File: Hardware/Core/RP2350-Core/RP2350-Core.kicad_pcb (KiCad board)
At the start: 2 copper layers, 9.1 x 7 mm, 60 parts, among them CN10 PR5L4015-5P-C-F, CN11 PR5L4015-5P-C-F, CN7 PR5L4015-5P-C-F, CN8 PR5L4015-5P-C-F, CN9 PR5L4015-5P-C-F, J7 SWD, J8 USB_C_Receptacle_USB2.0_14P, Q1 BSS123, Q3 BSS123, SW1 TS-1187A-B-A-B, SW2 TS-1187A-B-A-B, U1 RP2354B, U19 W25Q16JVSNIQ, U2 AP2112K-3.3, U3 LM66200DRLR, U35 PR5L5015-5P-C-H, U36 PR5L5015-5P-C-H, U37 PR5L5015-5P-C-H, U38 PR5L5015-5P-C-H, U39 PR5L5015-5P-C-H, Y1 Crystal

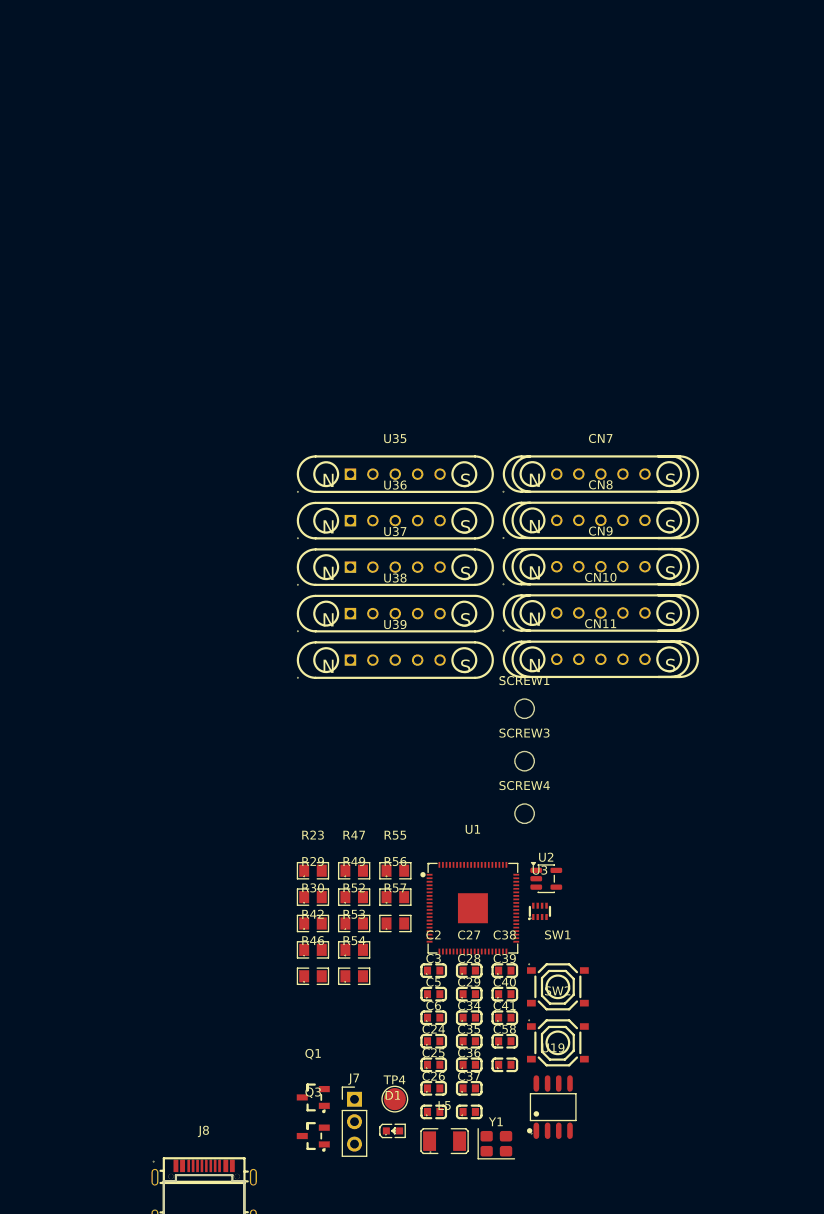
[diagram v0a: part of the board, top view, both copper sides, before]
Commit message: Footprint assigned core rp2350
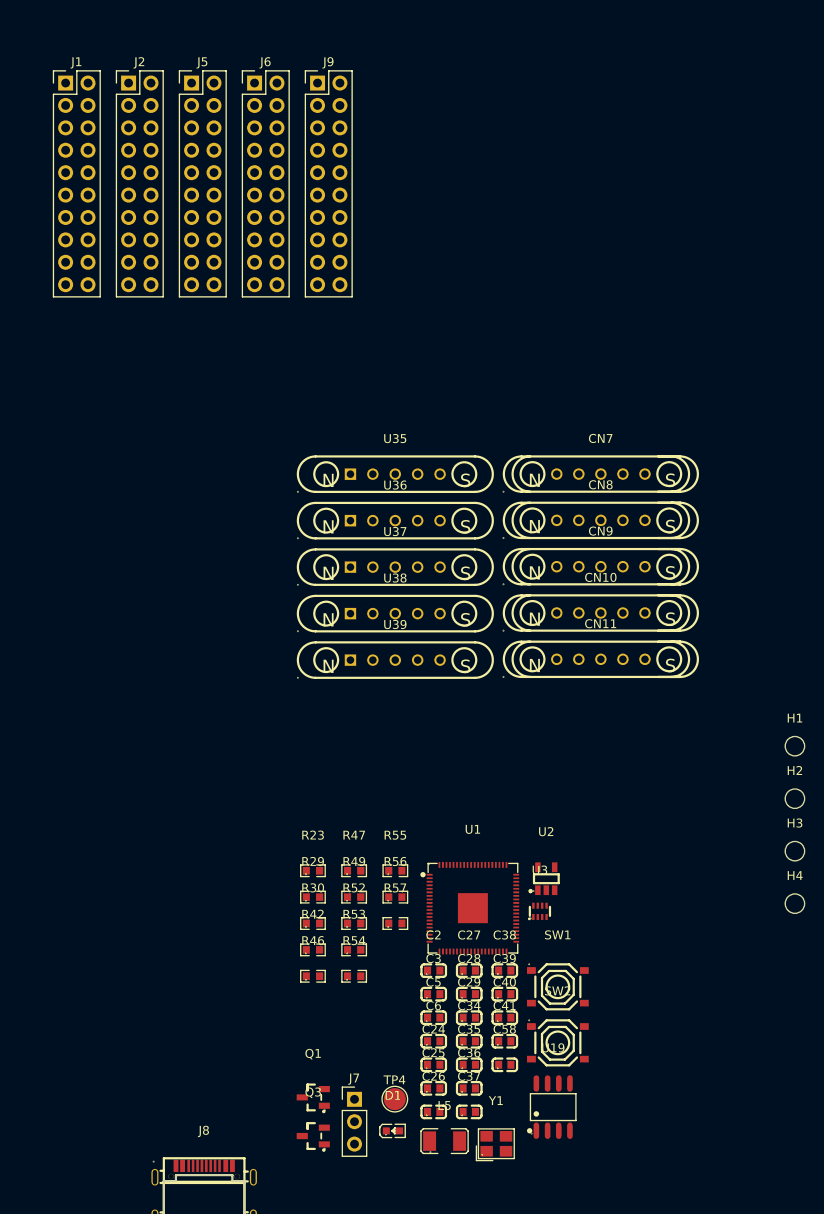
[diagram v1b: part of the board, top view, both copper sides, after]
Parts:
- removed SCREW1, SCREW3, SCREW4: ~, MountingHole:MountingHole_2.2mm_M2
- added H1: MountingHole, MountingHole:MountingHole_2.2mm_M2, F.Cu at (114.5, 98.0)
- added H2: MountingHole, MountingHole:MountingHole_2.2mm_M2, F.Cu at (114.5, 103.9)
- added H3: MountingHole, MountingHole:MountingHole_2.2mm_M2, F.Cu at (114.5, 109.9)
- added H4: MountingHole, MountingHole:MountingHole_2.2mm_M2, F.Cu at (114.5, 115.8)
- added J1: Conn_01x10_Socket, Connector_PinHeader_2.54mm:PinHeader_2x10_P2.54mm_Vertical, F.Cu at (31.8, 22.8)
- added J2: Conn_01x10_Socket, Connector_PinHeader_2.54mm:PinHeader_2x10_P2.54mm_Vertical, F.Cu at (38.9, 22.8)
- added J5: Conn_01x10_Socket, Connector_PinHeader_2.54mm:PinHeader_2x10_P2.54mm_Vertical, F.Cu at (46.1, 22.8)
- added J6: Conn_01x10_Socket, Connector_PinHeader_2.54mm:PinHeader_2x10_P2.54mm_Vertical, F.Cu at (53.2, 22.8)
- added J9: Conn_01x10_Socket, Connector_PinHeader_2.54mm:PinHeader_2x10_P2.54mm_Vertical, F.Cu at (60.4, 22.8)
- R23, R29, R30, R42, R46, R47, R49, R52, R53, R54, R55, R56, R57: footprint SpaghettiLAB:R0805 -> SpaghettiLAB:R0603
- U2: footprint Package_TO_SOT_SMD:SOT-23-5 -> SpaghettiLAB:SOT-25-5_L2.9-W1.6-P0.95-LS2.8-BL
- Y1: footprint Crystal:Crystal_SMD_3225-4Pin_3.2x2.5mm -> SpaghettiLAB:CRYSTAL-SMD_4P-L3.2-W2.5-BL

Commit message: Created rp2354 and rp2350 variants
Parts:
- added A1: Arduino_UNO_R3, Module:Arduino_UNO_R3, F.Cu at (142.1, 33.8)
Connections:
- net /InOut/ADC6_GPIO46 renamed /InOut (page 4)/ADC6_GPIO46
- net /InOut/ADC7_GPIO47 renamed /InOut (page 4)/ADC7_GPIO47
- net /InOut/FLEX0 renamed /InOut (page 4)/FLEX0
- net /InOut/FLEX1 renamed /InOut (page 4)/FLEX1
- net /InOut/FLEX2 renamed /InOut (page 4)/FLEX2
- net /InOut/FLEX3 renamed /InOut (page 4)/FLEX3
- net /InOut/FLEX4 renamed /InOut (page 4)/FLEX4
- net /InOut/FLEX5 renamed /InOut (page 4)/FLEX5
- net /InOut/FLEX6 renamed /InOut (page 4)/FLEX6
- net /InOut/GPIO0 renamed /InOut (page 4)/GPIO0
- net /InOut/GPIO1 renamed /InOut (page 4)/GPIO1
- net /InOut/GPIO13 renamed /InOut (page 4)/GPIO13
- net /InOut/GPIO14 renamed /InOut (page 4)/GPIO14
- net /InOut/GPIO15 renamed /InOut (page 4)/GPIO15
- net /InOut/GPIO18 renamed /InOut (page 4)/GPIO18
- net /InOut/GPIO19 renamed /InOut (page 4)/GPIO19
- net /InOut/GPIO2 renamed /InOut (page 4)/GPIO2
- net /InOut/GPIO20 renamed /InOut (page 4)/GPIO20
- net /InOut/GPIO21 renamed /InOut (page 4)/GPIO21
- net /InOut/GPIO22 renamed /InOut (page 4)/GPIO22
- net /InOut/GPIO23 renamed /InOut (page 4)/GPIO23
- net /InOut/GPIO24 renamed /InOut (page 4)/GPIO24
- net /InOut/GPIO25 renamed /InOut (page 4)/GPIO25
- net /InOut/GPIO26 renamed /InOut (page 4)/GPIO26
- net /InOut/GPIO27 renamed /InOut (page 4)/GPIO27
- net /InOut/GPIO28 renamed /InOut (page 4)/GPIO28
- net /InOut/GPIO29 renamed /InOut (page 4)/GPIO29
- net /InOut/GPIO30 renamed /InOut (page 4)/GPIO30
- net /InOut/GPIO31 renamed /InOut (page 4)/GPIO31
- net /InOut/GPIO32 renamed /InOut (page 4)/GPIO32
- net /InOut/GPIO33 renamed /InOut (page 4)/GPIO33
- net /InOut/GPIO34 renamed /InOut (page 4)/GPIO34
- net /InOut/GPIO35 renamed /InOut (page 4)/GPIO35
- net /InOut/GPIO36 renamed /InOut (page 4)/GPIO36
- net /InOut/GPIO37 renamed /InOut (page 4)/GPIO37
- net /InOut/GPIO38 renamed /InOut (page 4)/GPIO38
- net /InOut/GPIO4 renamed /InOut (page 4)/GPIO4
- net /InOut/ID renamed /InOut (page 4)/ID
- net /InOut/QSPI_SCLK renamed /InOut (page 4)/QSPI_SCLK
- net /InOut/QSPI_SD0 renamed /InOut (page 4)/QSPI_SD0
- net /InOut/QSPI_SD1 renamed /InOut (page 4)/QSPI_SD1
- net /InOut/QSPI_SD2 renamed /InOut (page 4)/QSPI_SD2
- net /InOut/QSPI_SD3 renamed /InOut (page 4)/QSPI_SD3
- net /InOut/QSPI_SS renamed /InOut (page 4)/QSPI_SS
- net /InOut/SCL_ALT renamed /InOut (page 4)/SCL_ALT
- net /InOut/SCL_AUX renamed /InOut (page 4)/SCL_AUX
- net /InOut/SDA_ALT renamed /InOut (page 4)/SDA_ALT
- net /InOut/SDA_AUX renamed /InOut (page 4)/SDA_AUX
- net /InOut/~{INT} renamed /InOut (page 4)/~{INT}
- net /InOut/~{RESET} renamed /InOut (page 4)/~{RESET}
- J6 pad 6: /InOut/ADC5_GPIO45 -> /InOut (page 4)/ADC5_GPIO45
- J6 pad 7: /InOut/ADC4_GPIO44 -> /InOut (page 4)/ADC4_GPIO44

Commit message: Verison RP2350 with arduino header support
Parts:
- removed J1, J2, J5, J6: Conn_01x10_Socket, Connector_PinHeader_2.54mm:PinHeader_2x10_P2.54mm_Vertical
- removed J8: USB_C_Receptacle_USB2.0_14P, SpaghettiLAB:USB-C-SMD_12P-P0.50-H-F_TYPE-C-31-M-14
- removed Q1: BSS123, SpaghettiLAB:SOT-23-3_L2.9-W1.5-P1.90-LS2.6-BR
- removed U1: RP2354B, SpaghettiLAB:QFN-80_L10.0-W10.0-P0.40-TL-EP3.4
- removed USBC1: TYPE-C-31-M-14, SpaghettiLAB:USB-C-SMD_12P-P0.50-H-F_TYPE-C-31-M-14
- added Q2: 2N7002, SpaghettiLAB:SOT-23-3_L2.9-W1.3-P1.90-LS2.4-BR, F.Cu at (158.1, 86.3)
- added U4: RP2350A, SpaghettiLAB:QFN-60_L7.0-W7.0-P0.40-TL-EP3.4, F.Cu at (169.0, 76.0)
- added USB1: TYPEC-324G-BCP24, SpaghettiLAB:USB-C-SMD_TYPEC-324G-BCP24, F.Cu at (161.5, 65.6)
- J9: footprint Connector_PinHeader_2.54mm:PinHeader_2x10_P2.54mm_Vertical -> Connector_PinHeader_2.54mm:PinHeader_2x05_P2.54mm_Vertical
- Q3: value BSS123 -> 2N7002; footprint SpaghettiLAB:SOT-23-3_L2.9-W1.5-P1.90-LS2.6-BR -> SpaghettiLAB:SOT-23-3_L2.9-W1.3-P1.90-LS2.4-BR
- moved J7 121.7 mm to (173.0, 82.8)
- moved TP4 121.6 mm to (169.2, 69.0)
- moved Q3 116.5 mm to (162.1, 86.3)
- moved D1 115.3 mm to (172.8, 91.5)
- moved J9 113.5 mm to (120.3, 119.2)
- moved L5 106.2 mm to (167.3, 90.7)
- moved U3 100.3 mm to (173.3, 68.2)
- moved U19 97.0 mm to (167.5, 84.6)
- moved U2 96.3 mm to (169.4, 64.4)
- moved Y1 94.2 mm to (158.9, 90.7)
- moved C34 94.1 mm to (150.0, 71.3)
- moved C38 94.1 mm to (154.1, 63.3)
- moved C39 94.1 mm to (154.1, 66.0)
- moved C40 94.1 mm to (154.1, 68.7)
- moved C41 94.1 mm to (154.1, 71.3)
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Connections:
- A1 pad 13: /InOut (page 4)/ADC4_GPIO44 -> /InOut (page 4)/SCL_ALT
- A1 pad 14: /InOut (page 4)/ADC5_GPIO45 -> /InOut (page 4)/SDA_ALT
- A1 pad 15: unconnected-(A1-D0/RX-Pad15) -> /InOut (page 4)/GPIO1
- A1 pad 16: unconnected-(A1-D1/TX-Pad16) -> /InOut (page 4)/GPIO0
- A1 pad 17: unconnected-(A1-D2-Pad17) -> /InOut (page 4)/GPIO2
- A1 pad 18: unconnected-(A1-D3-Pad18) -> /InOut (page 4)/GPIO4
- A1 pad 19: unconnected-(A1-D4-Pad19) -> /InOut (page 4)/GPIO13
- A1 pad 2: unconnected-(A1-IOREF-Pad2) -> +3V3
- A1 pad 20: unconnected-(A1-D5-Pad20) -> /InOut (page 4)/GPIO14
- A1 pad 21: unconnected-(A1-D6-Pad21) -> /InOut (page 4)/GPIO15
- A1 pad 22: unconnected-(A1-D7-Pad22) -> /InOut (page 4)/GPIO18
- A1 pad 23: unconnected-(A1-D8-Pad23) -> /InOut (page 4)/GPIO19
- A1 pad 24: unconnected-(A1-D9-Pad24) -> /InOut (page 4)/GPIO20
- A1 pad 25: unconnected-(A1-D10-Pad25) -> /InOut (page 4)/GPIO21
- A1 pad 26: unconnected-(A1-D11-Pad26) -> /InOut (page 4)/GPIO22
- A1 pad 27: unconnected-(A1-D12-Pad27) -> /InOut (page 4)/GPIO23
- A1 pad 28: unconnected-(A1-D13-Pad28) -> /InOut (page 4)/GPIO24
- A1 pad 3: unconnected-(A1-~{RESET}-Pad3) -> /InOut (page 4)/~{RESET}
- A1 pad 30: unconnected-(A1-AREF-Pad30) -> +3V3
- A1 pad 4: unconnected-(A1-3V3-Pad4) -> VLOGIC
- A1 pad 5: unconnected-(A1-+5V-Pad5) -> 5V
- A1 pad 8: unconnected-(A1-VIN-Pad8) -> VHV
- SW2 pad 1: Net-(SW2-A) -> /InOut (page 4)/~{RESET}
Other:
- board outline removed
